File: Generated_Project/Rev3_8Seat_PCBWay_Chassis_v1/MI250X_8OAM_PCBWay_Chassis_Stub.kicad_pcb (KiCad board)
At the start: 12 copper layers, 492 x 372 mm, 49 parts, among them J0_Conn0 218910-1115, J0_Conn1 218910-1115, J1_Conn0 218910-1115, J1_Conn1 218910-1115, J2_Conn0 218910-1115, J2_Conn1 218910-1115, J3_Conn0 218910-1115, J3_Conn1 218910-1115, J4_Conn0 218910-1115, J4_Conn1 218910-1115, J5_Conn0 218910-1115, J5_Conn1 218910-1115, J6_Conn0 218910-1115, J6_Conn1 218910-1115, J7_Conn0 218910-1115, J7_Conn1 218910-1115

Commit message: Make PM8536B-FEI the PRIMARY switch keepout (DNP x2).
Two 37.5 mm 1311-FCBGA courtyards, x8 per GCD (SW0 seats 0-3, SW1 4-7),
two CPU x16 uplinks. PEX8780 stays a cheaper 80-lane alt in docs only.
GCD1 = SERDES_7 remains Inferred. No CEM, no xGMI, do not fabricate.

Co-authored-by: zivzancoeli-commits <zivzancoeli-commits@users.noreply.github.com>
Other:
- board text added: "12L 2.0mm stuffed-switch TARGET. 8L 2.0mm is cheaper DNP option only. PEX8780 docs-only. No signal tracks."
- board text added: "Molex 218910-1115 x16 | 12L 2.0mm TARGET | LOCAL P48V pours | 2x PM8536B-FEI DNP | SB175 star | NOT a UBB"
- board text added: "PM8536B-FEI 37.5mm 1311-FCBGA"
- board text added: "SEAT 0 ELEC NAMED first-stuff OK PE->SW0 x8/GCD"
- board text added: "SEAT 1 ELEC NAMED first-stuff OK PE->SW0 x8/GCD"
- board text added: "SEAT 2 ELEC NAMED module DNP OK PE->SW0 no respin"
- board text added: "SEAT 3 ELEC NAMED module DNP OK PE->SW0 no respin"
- board text added: "SEAT 4 ELEC NAMED module DNP OK PE->SW1 no respin"
- board text added: "SEAT 5 ELEC NAMED module DNP OK PE->SW1 no respin"
- board text added: "SEAT 6 ELEC NAMED module DNP OK PE->SW1 no respin"
- board text added: "SEAT 7 ELEC NAMED module DNP OK PE->SW1 no respin"
- board text added: "U_SW0 DNP PRIMARY"
- board text added: "U_SW1 DNP PRIMARY"
- board text added: "X11DPH-T two CPU x16 uplinks"
- board text added: "seats 0-3 x8/GCD 16US+64DS"
- board text added: "seats 4-7 x8/GCD 16US+64DS"
- board text removed: "35mm 1156-FCBGA 80-lane"
- board text removed: "8x x8 + one x16 UL NOT stuffed"
- board text removed: "Molex 218910-1115 x16 | PEX8780-AB80BI G CANDIDATE DNP | 8L likely if stuffed | SB175 star | NOT a UBB"
- board text removed: "NO SECOND SWITCH MPN"
- board text removed: "PEX8780 CANDIDATE DNP. 8L likely if 1156 stuffed. PCBWay 1156 assembly Unknown. No signal tracks."
- board text removed: "PEX8780-AB80BI G"
- board text removed: "PEX8796 / PEX88096 / PM40100 not placed"
- board text removed: "SEAT 0 ELEC NAMED first-stuff OK PE->PEX8780 x8"
- board text removed: "SEAT 1 ELEC NAMED first-stuff OK PE->PEX8780 x8"
- board text removed: "SEAT 2 ELEC NAMED module DNP OK PE->PEX8780 x8 no respin"
- board text removed: "SEAT 3 ELEC NAMED module DNP OK PE->PEX8780 x8 no respin"
- board text removed: "SEAT 4 ELEC NAMED module DNP OK PE->PEX8780 x8 no respin"
- board text removed: "SEAT 5 ELEC NAMED module DNP OK PE->PEX8780 x8 no respin"
- board text removed: "SEAT 6 ELEC NAMED module DNP OK PE->PEX8780 x8 no respin"
- board text removed: "SEAT 7 ELEC NAMED module DNP OK PE->PEX8780 x8 no respin"
- board text removed: "U_SW CANDIDATE DNP"
- board text removed: "X11DPH-T one CPU x16 uplink"
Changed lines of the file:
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@@
     (rev "Rev3_8Seat_PCBWay_v1")
     (comment 1 "DO NOT FABRICATE. DO NOT ENERGIZE P48V. Molex 60V written; 1.2A/contact OPEN.")
-    (comment 2 "492 x 372 mm. PEX8780-AB80BI G CANDIDATE DNP. 8L likely if stuffed. SB175.")
+    (comment 2 "492 x 372 mm 12-layer 2.0 mm stuffed-switch TARGET. Local P48V. 2x PM8536 DNP PRIMARY. SB175.")
   )
   (layers
@@
     (at 246.000 6) (layer "F.SilkS")
     (effects (font (size 2.4 2.4) (thickness 0.3))))
-  (gr_text "Molex 218910-1115 x16  |  PEX8780-AB80BI G CANDIDATE DNP  |  8L likely if stuffed  |  SB175 star  |  NOT a UBB"
+  (gr_text "Molex 218910-1115 x16  |  12L 2.0mm TARGET  |  LOCAL P48V pours  |  2x PM8536B-FEI DNP  |  SB175 star  |  NOT a UBB"
     (at 246.000 12) (layer "F.SilkS")
     (effects (font (size 1.5 1.5) (thickness 0.18))))
@@
   (gr_rect (start 20.500 20.500) (end 122.500 185.500)
     (stroke (width 0.12) (type dash)) (fill none) (layer "Dwgs.User"))
-  (gr_text "SEAT 0  ELEC NAMED  first-stuff OK  PE->PEX8780  x8"
+  (gr_text "SEAT 0  ELEC NAMED  first-stuff OK  PE->SW0  x8/GCD"
     (at 71.500 28.000) (layer "F.SilkS")
     (effects (font (size 1.5 1.5) (thickness 0.18))))
@@
   (gr_rect (start 123.500 20.500) (end 225.500 185.500)
     (stroke (width 0.12) (type dash)) (fill none) (layer "Dwgs.User"))
-  (gr_text "SEAT 1  ELEC NAMED  first-stuff OK  PE->PEX8780  x8"
+  (gr_text "SEAT 1  ELEC NAMED  first-stuff OK  PE->SW0  x8/GCD"
     (at 174.500 28.000) (layer "F.SilkS")
     (effects (font (size 1.5 1.5) (thickness 0.18))))
@@
   (gr_rect (start 226.500 20.500) (end 328.500 185.500)
     (stroke (width 0.12) (type dash)) (fill none) (layer "Dwgs.User"))
-  (gr_text "SEAT 2  ELEC NAMED  module DNP OK  PE->PEX8780  x8  no respin"
+  (gr_text "SEAT 2  ELEC NAMED  module DNP OK  PE->SW0  no respin"
     (at 277.500 28.000) (layer "F.SilkS")
     (effects (font (size 1.5 1.5) (thickness 0.18))))
@@
   (gr_rect (start 329.500 20.500) (end 431.500 185.500)
     (stroke (width 0.12) (type dash)) (fill none) (layer "Dwgs.User"))
-  (gr_text "SEAT 3  ELEC NAMED  module DNP OK  PE->PEX8780  x8  no respin"
+  (gr_text "SEAT 3  ELEC NAMED  module DNP OK  PE->SW0  no respin"
     (at 380.500 28.000) (layer "F.SilkS")
     (effects (font (size 1.5 1.5) (thickness 0.18))))
@@
   (gr_rect (start 20.500 186.500) (end 122.500 351.500)
     (stroke (width 0.12) (type dash)) (fill none) (layer "Dwgs.User"))
-  (gr_text "SEAT 4  ELEC NAMED  module DNP OK  PE->PEX8780  x8  no respin"
+  (gr_text "SEAT 4  ELEC NAMED  module DNP OK  PE->SW1  no respin"
     (at 71.500 194.000) (layer "F.SilkS")
     (effects (font (size 1.5 1.5) (thickness 0.18))))
@@
   (gr_rect (start 123.500 186.500) (end 225.500 351.500)
     (stroke (width 0.12) (type dash)) (fill none) (layer "Dwgs.User"))
-  (gr_text "SEAT 5  ELEC NAMED  module DNP OK  PE->PEX8780  x8  no respin"
+  (gr_text "SEAT 5  ELEC NAMED  module DNP OK  PE->SW1  no respin"
     (at 174.500 194.000) (layer "F.SilkS")
     (effects (font (size 1.5 1.5) (thickness 0.18))))
@@
   (gr_rect (start 226.500 186.500) (end 328.500 351.500)
     (stroke (width 0.12) (type dash)) (fill none) (layer "Dwgs.User"))
-  (gr_text "SEAT 6  ELEC NAMED  module DNP OK  PE->PEX8780  x8  no respin"
+  (gr_text "SEAT 6  ELEC NAMED  module DNP OK  PE->SW1  no respin"
     (at 277.500 194.000) (layer "F.SilkS")
     (effects (font (size 1.5 1.5) (thickness 0.18))))
@@
   (gr_rect (start 329.500 186.500) (end 431.500 351.500)
     (stroke (width 0.12) (type dash)) (fill none) (layer "Dwgs.User"))
-  (gr_text "SEAT 7  ELEC NAMED  module DNP OK  PE->PEX8780  x8  no respin"
+  (gr_text "SEAT 7  ELEC NAMED  module DNP OK  PE->SW1  no respin"
     (at 380.500 194.000) (layer "F.SilkS")
     (effects (font (size 1.5 1.5) (thickness 0.18))))
@@
   (gr_rect (start 452.000 28.000) (end 492.000 68.000)
     (stroke (width 0.2) (type dash)) (fill none) (layer "Dwgs.User"))
-  (gr_text "U_SW CANDIDATE DNP"
+  (gr_text "U_SW0 DNP PRIMARY"
     (at 472.000 48.000 90) (layer "F.SilkS")
     (effects (font (size 1.3 1.3) (thickness 0.16))))
-  (gr_text "PEX8780-AB80BI G"
+  (gr_text "PM8536B-FEI 37.5mm 1311-FCBGA"
     (at 480.000 48.000 90) (layer "F.SilkS")
-    (effects (font (size 1.1 1.1) (thickness 0.14))))
-  (gr_text "35mm 1156-FCBGA  80-lane"
+    (effects (font (size 1.0 1.0) (thickness 0.12))))
+  (gr_text "seats 0-3  x8/GCD  16US+64DS"
     (at 488.000 48.000 90) (layer "F.SilkS")
     (effects (font (size 0.9 0.9) (thickness 0.1))))
-  (gr_text "8x x8 + one x16 UL  NOT stuffed"
-    (at 496.000 48.000 90) (layer "F.SilkS")
-    (effects (font (size 0.85 0.85) (thickness 0.1))))
   (gr_rect (start 452.000 90.000) (end 492.000 250.000)
     (stroke (width 0.2) (type dash)) (fill none) (layer "F.CrtYd"))
@@
     (at 472.000 170.000 90) (layer "F.SilkS")
     (effects (font (size 1.5 1.5) (thickness 0.18))))
-  (gr_text "X11DPH-T one CPU x16 uplink"
+  (gr_text "X11DPH-T two CPU x16 uplinks"
     (at 464.000 170.000 90) (layer "F.SilkS")
     (effects (font (size 1.1 1.1) (thickness 0.14))))
@@
     (at 488.000 170.000 90) (layer "F.SilkS")
     (effects (font (size 1.1 1.1) (thickness 0.14))))
-  (gr_text "NO SECOND SWITCH MPN"
+  (gr_rect (start 452.000 284.000) (end 492.000 324.000)
+    (stroke (width 0.25) (type dash)) (fill none) (layer "F.CrtYd"))
+  (gr_rect (start 452.000 284.000) (end 492.000 324.000)
+    (stroke (width 0.2) (type dash)) (fill none) (layer "Dwgs.User"))
+  (gr_text "U_SW1 DNP PRIMARY"
     (at 472.000 304.000 90) (layer "F.SilkS")
-    (effects (font (size 1.2 1.2) (thickness 0.14))))
-  (gr_text "PEX8796 / PEX88096 / PM40100 not placed"
-    (at 482.000 304.000 90) (layer "F.SilkS")
-    (effects (font (size 0.85 0.85) (thickness 0.1))))
+    (effects (font (size 1.3 1.3) (thickness 0.16))))
+  (gr_text "PM8536B-FEI 37.5mm 1311-FCBGA"
+    (at 480.000 304.000 90) (layer "F.SilkS")
+    (effects (font (size 1.0 1.0) (thickness 0.12))))
+  (gr_text "seats 4-7  x8/GCD  16US+64DS"
+    (at 488.000 304.000 90) (layer "F.SilkS")
+    (effects (font (size 0.9 0.9) (thickness 0.1))))
   (gr_text "STAR-FED P48V — LOCAL POURS ONLY — DO NOT ENERGIZE"
     (at 246.000 360.000) (layer "F.SilkS")
     (effects (font (size 1.8 1.8) (thickness 0.22))))
-  (gr_text "PEX8780 CANDIDATE DNP. 8L likely if 1156 stuffed. PCBWay 1156 assembly Unknown. No signal tracks."
+  (gr_text "12L 2.0mm stuffed-switch TARGET. 8L 2.0mm is cheaper DNP option only. PEX8780 docs-only. No signal tracks."
     (at 246.000 16.5) (layer "Cmts.User")
-    (effects (font (size 1.2 1.2) (thickness 0.14))))
+    (effects (font (size 1.1 1.1) (thickness 0.12))))
   (gr_text "Seat grid: row0 (Y=20) seats 0-3; row1 (Y=186) seats 4-7; col pitch 103 mm. Conn rotation 180 Inferred."
     (at 246.000 354.000) (layer "Cmts.User")
@@
   )
   (zone (net 0) (net_name "") (layers "*.Cu")
+    (hatch edge 0.5)
+    (priority 0)
+    (keepout (tracks not_allowed) (vias not_allowed) (pads allowed) (copperpour not_allowed) (footprints not_allowed))
+    (fill yes (thermal_gap 0.5) (thermal_bridge_width 0.5))
+    (polygon (pts (xy 452.000 284.000) (xy 492.000 284.000) (xy 492.000 324.000) (xy 452.000 324.000)))
+  )
+  (zone (net 0) (net_name "") (layers "*.Cu")

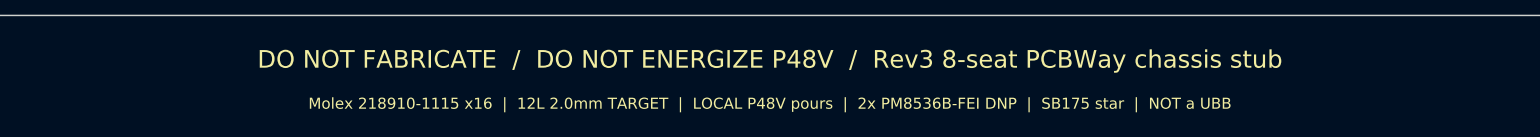
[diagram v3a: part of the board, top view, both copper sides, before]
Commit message: Regenerate 8-seat named-net chassis: all seats electrically designed.
Sheet names seats 2-7 are connectors, not MechPower. Silk/title say named-net
chassis. KiCad 9.0.9 ERC/DRC and top preview refreshed. Do not fabricate,
do not energize P48V, do not upload to PCBWay.

Co-authored-by: zivzancoeli-commits <zivzancoeli-commits@users.noreply.github.com>
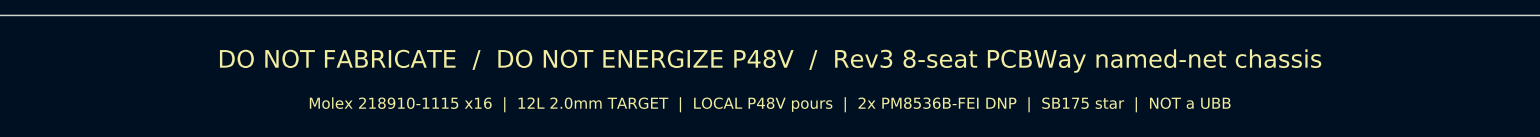
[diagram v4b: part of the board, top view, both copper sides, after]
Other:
- board text added: "DO NOT FABRICATE / DO NOT ENERGIZE P48V / Rev3 8-seat PCBWay named-net chassis"
- board text removed: "DO NOT FABRICATE / DO NOT ENERGIZE P48V / Rev3 8-seat PCBWay chassis stub"
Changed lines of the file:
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@@
   (paper "A1")
   (title_block
-    (title "DO NOT FABRICATE — Rev3 8-seat PCBWay chassis stub")
-    (date "2026-08-21")
+    (title "DO NOT FABRICATE — Rev3 8-seat PCBWay named-net chassis")
+    (date "2026-08-22")
     (rev "Rev3_8Seat_PCBWay_v1")
     (comment 1 "DO NOT FABRICATE. DO NOT ENERGIZE P48V. Molex 60V written; 1.2A/contact OPEN.")
@@
   (gr_rect (start 0 0) (end 492.000 372.000)
     (stroke (width 0.2) (type solid)) (fill none) (layer "Edge.Cuts"))
-  (gr_text "DO NOT FABRICATE  /  DO NOT ENERGIZE P48V  /  Rev3 8-seat PCBWay chassis stub"
+  (gr_text "DO NOT FABRICATE  /  DO NOT ENERGIZE P48V  /  Rev3 8-seat PCBWay named-net chassis"
     (at 246.000 6) (layer "F.SilkS")
     (effects (font (size 2.4 2.4) (thickness 0.3))))

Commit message: Add PCBWay-submittable POWER+MECH fab package for the Rev3 8-seat chassis.
Star-fed P48V (SB175 6325G1 + 2x 1382, per-seat 0476015.MR, local Conn0 pours),
THL 40-4812WI and OKI-78SR bucks, filled 12L 2.0 mm Gerbers/drill/IPC-356/PnP.
PM8536 stays DNP. Silk keeps DO NOT ENERGIZE P48V. Do not upload from this agent.

Co-authored-by: zivzancoeli-commits <zivzancoeli-commits@users.noreply.github.com>
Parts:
- added F0: 0476015.MR, footprints:Fuse_Littelfuse-NANO2-451_453, F.Cu at (52.0, 169.5)
- added F1: 0476015.MR, footprints:Fuse_Littelfuse-NANO2-451_453, F.Cu at (155.1, 169.5)
- added F2: 0476015.MR, footprints:Fuse_Littelfuse-NANO2-451_453, F.Cu at (258.1, 169.5)
- added F3: 0476015.MR, footprints:Fuse_Littelfuse-NANO2-451_453, F.Cu at (361.1, 169.5)
- added F4: 0476015.MR, footprints:Fuse_Littelfuse-NANO2-451_453, F.Cu at (105.0, 332.0)
- added F5: 0476015.MR, footprints:Fuse_Littelfuse-NANO2-451_453, F.Cu at (155.1, 336.0)
- added F6: 0476015.MR, footprints:Fuse_Littelfuse-NANO2-451_453, F.Cu at (258.1, 336.0)
- added F7: 0476015.MR, footprints:Fuse_Littelfuse-NANO2-451_453, F.Cu at (361.1, 336.0)
- added F_P12: 0476002.MR, footprints:Fuse_Littelfuse-NANO2-451_453, F.Cu at (448.0, 336.0)
- added U_P12V1: THL 40-4812WI, footprints:Converter_DCDC_TRACO_THL40-xxxxWI_THT, F.Cu at (470.0, 330.0)
- added U_P3V3: OKI-78SR-3.3/1.5-W36-C, footprints:Converter_DCDC_Murata_OKI-78SR_Vertical, F.Cu at (454.0, 366.0)
- J_SB175: value SB175_175A_600V -> 6325G1_SB175
- moved J_SB175 8.00 mm to (70.0, 354.0)
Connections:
- J1_Conn0 pad H59: P48V -> P48V_S1
- J1_Conn0 pad H60: P48V -> P48V_S1
- J1_Conn0 pad H61: P48V -> P48V_S1
- J1_Conn0 pad H62: P48V -> P48V_S1
- J1_Conn0 pad H63: P48V -> P48V_S1
- J1_Conn0 pad H64: P48V -> P48V_S1
- J1_Conn0 pad J61: P48V -> P48V_S1
- J1_Conn0 pad J62: P48V -> P48V_S1
- J1_Conn0 pad J63: P48V -> P48V_S1
- J1_Conn0 pad J64: P48V -> P48V_S1
- J1_Conn0 pad K59: P48V -> P48V_S1
- J1_Conn0 pad K60: P48V -> P48V_S1
- J1_Conn0 pad K61: P48V -> P48V_S1
- J1_Conn0 pad K62: P48V -> P48V_S1
- J1_Conn0 pad L61: P48V -> P48V_S1
- J1_Conn0 pad L62: P48V -> P48V_S1
- J2_Conn0 pad H59: P48V -> P48V_S2
- J2_Conn0 pad H60: P48V -> P48V_S2
- J2_Conn0 pad H61: P48V -> P48V_S2
- J2_Conn0 pad H62: P48V -> P48V_S2
- J2_Conn0 pad H63: P48V -> P48V_S2
- J2_Conn0 pad H64: P48V -> P48V_S2
- J2_Conn0 pad J61: P48V -> P48V_S2
- J2_Conn0 pad J62: P48V -> P48V_S2
- J2_Conn0 pad J63: P48V -> P48V_S2
- J2_Conn0 pad J64: P48V -> P48V_S2
- J2_Conn0 pad K59: P48V -> P48V_S2
- J2_Conn0 pad K60: P48V -> P48V_S2
- J2_Conn0 pad K61: P48V -> P48V_S2
- J2_Conn0 pad K62: P48V -> P48V_S2
- J2_Conn0 pad L61: P48V -> P48V_S2
- J2_Conn0 pad L62: P48V -> P48V_S2
- J3_Conn0 pad H59: P48V -> P48V_S3
- J3_Conn0 pad H60: P48V -> P48V_S3
- J3_Conn0 pad H61: P48V -> P48V_S3
- J3_Conn0 pad H62: P48V -> P48V_S3
- J3_Conn0 pad H63: P48V -> P48V_S3
- J3_Conn0 pad H64: P48V -> P48V_S3
- J3_Conn0 pad J61: P48V -> P48V_S3
- J3_Conn0 pad J62: P48V -> P48V_S3
- J3_Conn0 pad J63: P48V -> P48V_S3
- J3_Conn0 pad J64: P48V -> P48V_S3
- J3_Conn0 pad K59: P48V -> P48V_S3
- J3_Conn0 pad K60: P48V -> P48V_S3
- J3_Conn0 pad K61: P48V -> P48V_S3
- J3_Conn0 pad K62: P48V -> P48V_S3
- J3_Conn0 pad L61: P48V -> P48V_S3
- J3_Conn0 pad L62: P48V -> P48V_S3
- J4_Conn0 pad H59: P48V -> P48V_S4
- J4_Conn0 pad H60: P48V -> P48V_S4
- J4_Conn0 pad H61: P48V -> P48V_S4
- J4_Conn0 pad H62: P48V -> P48V_S4
- J4_Conn0 pad H63: P48V -> P48V_S4
- J4_Conn0 pad H64: P48V -> P48V_S4
- J4_Conn0 pad J61: P48V -> P48V_S4
- J4_Conn0 pad J62: P48V -> P48V_S4
- J4_Conn0 pad J63: P48V -> P48V_S4
- J4_Conn0 pad J64: P48V -> P48V_S4
- J4_Conn0 pad K59: P48V -> P48V_S4
- J4_Conn0 pad K60: P48V -> P48V_S4
- J4_Conn0 pad K61: P48V -> P48V_S4
- J4_Conn0 pad K62: P48V -> P48V_S4
- J4_Conn0 pad L61: P48V -> P48V_S4
- J4_Conn0 pad L62: P48V -> P48V_S4
- J5_Conn0 pad H59: P48V -> P48V_S5
- J5_Conn0 pad H60: P48V -> P48V_S5
- J5_Conn0 pad H61: P48V -> P48V_S5
- J5_Conn0 pad H62: P48V -> P48V_S5
- J5_Conn0 pad H63: P48V -> P48V_S5
- J5_Conn0 pad H64: P48V -> P48V_S5
- J5_Conn0 pad J61: P48V -> P48V_S5
- J5_Conn0 pad J62: P48V -> P48V_S5
- J5_Conn0 pad J63: P48V -> P48V_S5
- J5_Conn0 pad J64: P48V -> P48V_S5
- J5_Conn0 pad K59: P48V -> P48V_S5
- J5_Conn0 pad K60: P48V -> P48V_S5
- J5_Conn0 pad K61: P48V -> P48V_S5
- J5_Conn0 pad K62: P48V -> P48V_S5
- J5_Conn0 pad L61: P48V -> P48V_S5
- J5_Conn0 pad L62: P48V -> P48V_S5
- J6_Conn0 pad H59: P48V -> P48V_S6
- J6_Conn0 pad H60: P48V -> P48V_S6
- J6_Conn0 pad H61: P48V -> P48V_S6
- J6_Conn0 pad H62: P48V -> P48V_S6
- J6_Conn0 pad H63: P48V -> P48V_S6
- J6_Conn0 pad H64: P48V -> P48V_S6
- J6_Conn0 pad J61: P48V -> P48V_S6
- J6_Conn0 pad J62: P48V -> P48V_S6
- J6_Conn0 pad J63: P48V -> P48V_S6
- J6_Conn0 pad J64: P48V -> P48V_S6
- J6_Conn0 pad K59: P48V -> P48V_S6
- J6_Conn0 pad K60: P48V -> P48V_S6
- J6_Conn0 pad K61: P48V -> P48V_S6
- J6_Conn0 pad K62: P48V -> P48V_S6
- J6_Conn0 pad L61: P48V -> P48V_S6
- J6_Conn0 pad L62: P48V -> P48V_S6
- J7_Conn0 pad H59: P48V -> P48V_S7
- J7_Conn0 pad H60: P48V -> P48V_S7
- J7_Conn0 pad H61: P48V -> P48V_S7
- J7_Conn0 pad H62: P48V -> P48V_S7
- J7_Conn0 pad H63: P48V -> P48V_S7
- J7_Conn0 pad H64: P48V -> P48V_S7
- J7_Conn0 pad J61: P48V -> P48V_S7
- J7_Conn0 pad J62: P48V -> P48V_S7
- J7_Conn0 pad J63: P48V -> P48V_S7
- J7_Conn0 pad J64: P48V -> P48V_S7
- J7_Conn0 pad K59: P48V -> P48V_S7
- J7_Conn0 pad K60: P48V -> P48V_S7
- J7_Conn0 pad K61: P48V -> P48V_S7
- J7_Conn0 pad K62: P48V -> P48V_S7
- J7_Conn0 pad L61: P48V -> P48V_S7
- J7_Conn0 pad L62: P48V -> P48V_S7
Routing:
- net P3V3: track 0.00 -> 2108.8 mm, vias 0 -> 10
- net P12V1: track 0.00 -> 1447.6 mm, vias 0 -> 10
- net GND: vias 0 -> 32
- added copper zone on F.Cu, net GND
- added copper zone on F.Cu, net P12V1
- added copper zone on B.Cu, net P3V3
- added copper zone on F.Cu, net P3V3
- added copper zone on F.Cu, net P48V_BRICK
- added copper zone on F.Cu, net P48V_S1
- added copper zone on F.Cu, net P48V_S2
- added copper zone on F.Cu, net P48V_S3
- added copper zone on F.Cu, net P48V_S4
- added copper zone on F.Cu, net P48V_S5
- added copper zone on F.Cu, net P48V_S6
- added copper zone on F.Cu, net P48V_S7
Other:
- board text added: "DO NOT ENERGIZE P48V / Rev3 8-seat PCBWay POWER+MECH first article"
- board text added: "F0 0476015.MR 15A"
- board text added: "F1 0476015.MR 15A"
- board text added: "F2 0476015.MR 15A"
- board text added: "F3 0476015.MR 15A"
- board text added: "F4 0476015.MR 15A"
- board text added: "F5 0476015.MR 15A"
- board text added: "F6 0476015.MR 15A"
- board text added: "F7 0476015.MR 15A"
- board text added: "F_P12 0476002.MR 2A"
- board text added: "STAR spines — not a 100A flood — DO NOT ENERGIZE"
- board text added: "U_P12V1 THL 40-4812WI 40W from 48V"
- board text added: "U_P3V3 OKI-78SR 3.3V 1.5A from P12V1"
- board text removed: "DO NOT FABRICATE / DO NOT ENERGIZE P48V / Rev3 8-seat PCBWay named-net chassis"
- board text removed: "P12V1 in <=50W MPN Unknown no VRM"
- board text removed: "P3V3 in <=5W MPN Unknown no VRM"
- board text removed: "~15A FUSE S0 MPN Unknown"
- board text removed: "~15A FUSE S1 MPN Unknown"
- board text removed: "~15A FUSE S2 MPN Unknown"
- board text removed: "~15A FUSE S3 MPN Unknown"
- board text removed: "~15A FUSE S4 MPN Unknown"
- board text removed: "~15A FUSE S5 MPN Unknown"
- board text removed: "~15A FUSE S6 MPN Unknown"
- board text removed: "~15A FUSE S7 MPN Unknown"
